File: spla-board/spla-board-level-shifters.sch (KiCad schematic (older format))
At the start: 20 parts, among them J3 J_BODGE, J6 J_SAMPLE, U15 74LVC8T245-Q1, U16 74LVC8T245-Q1, U17 74LVC8T245-Q1, U20 74LVC8T245-Q1, U22 74LVC8T245-Q1, U23 74LVC8T245-Q1, U24 74LVC8T245-Q1, U25 74LVC8T245-Q1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

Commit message: schematic/pch: Remove '-Q1' suffix from 74LVC8T245 chips.
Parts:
- U15, U16, U17, U20, U22, U23, U24, U25, U26, U27, U28, U29, U30, U31, U32: value 74LVC8T245-Q1 -> 74LVC8T245; symbol SPLA:74LVC8T245-Q1 -> SPLA:74LVC8T245
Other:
- note removed: "TODO: Rearrange these pins for PCB layout."
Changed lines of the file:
@@
 FPGA_~PAWR~
 $Comp
-L SPLA:74LVC8T245-Q1 U23
+L SPLA:74LVC8T245 U23
 U 1 1 5E550799
 P 2400 9500
 F 0 "U23" H 2100 8850 50  0000 L CNN
-F 1 "74LVC8T245-Q1" V 2400 9500 50  0000 C CNN
+F 1 "74LVC8T245" V 2400 9500 50  0000 C CNN
 F 2 "Package_SO:TSSOP-24_4.4x7.8mm_P0.65mm" H 2400 8750 50  0001 C CNN
-F 3 "www.ti.com/lit/ds/symlink/txs0108e.pdf" H 2400 9400 50  0001 C CNN
+F 3 "" H 2400 9400 50  0001 C CNN
 	1    2400 9500
 	1    0    0    -1
 $EndComp
 $Comp
-L SPLA:74LVC8T245-Q1 U22
+L SPLA:74LVC8T245 U22
 U 1 1 5E55EB1D
 P 2400 7000
 F 0 "U22" H 2400 7750 50  0000 C CNN
-F 1 "74LVC8T245-Q1" V 2400 6950 50  0000 C CNN
+F 1 "74LVC8T245" V 2400 6950 50  0000 C CNN
 F 2 "Package_SO:TSSOP-24_4.4x7.8mm_P0.65mm" H 2400 5700 50  0001 C CNN
-F 3 "www.ti.com/lit/ds/symlink/txs0108e.pdf" H 2400 7150 50  0001 C CNN
+F 3 "" H 2400 7150 50  0001 C CNN
 	1    2400 7000
 	1    0    0    -1
@@
 FPGA_PA7
 $Comp
-L SPLA:74LVC8T245-Q1 U26
+L SPLA:74LVC8T245 U26
 U 1 1 5E56FCA9
 P 8750 7000
 F 0 "U26" H 8750 7750 50  0000 C CNN
-F 1 "74LVC8T245-Q1" V 8750 6950 50  0000 C CNN
+F 1 "74LVC8T245" V 8750 6950 50  0000 C CNN
 F 2 "Package_SO:TSSOP-24_4.4x7.8mm_P0.65mm" H 8750 5700 50  0001 C CNN
-F 3 "www.ti.com/lit/ds/symlink/txs0108e.pdf" H 8750 7150 50  0001 C CNN
+F 3 "" H 8750 7150 50  0001 C CNN
 	1    8750 7000
 	1    0    0    -1
@@
 Peripheral Bus
 $Comp
-L SPLA:74LVC8T245-Q1 U24
+L SPLA:74LVC8T245 U24
 U 1 1 5E5C1563
 P 6300 7000
 F 0 "U24" H 6300 7750 50  0000 C CNN
-F 1 "74LVC8T245-Q1" V 6300 6950 50  0000 C CNN
+F 1 "74LVC8T245" V 6300 6950 50  0000 C CNN
 F 2 "Package_SO:TSSOP-24_4.4x7.8mm_P0.65mm" H 6300 5700 50  0001 C CNN
-F 3 "www.ti.com/lit/ds/symlink/txs0108e.pdf" H 6300 7150 50  0001 C CNN
+F 3 "" H 6300 7150 50  0001 C CNN
 	1    6300 7000
 	1    0    0    -1
@@
 FPGA_VAA7
 $Comp
-L SPLA:74LVC8T245-Q1 U25
+L SPLA:74LVC8T245 U25
 U 1 1 5E5CA87C
 P 6300 9500
 F 0 "U25" H 6300 10250 50  0000 C CNN
-F 1 "74LVC8T245-Q1" V 6300 9450 50  0000 C CNN
+F 1 "74LVC8T245" V 6300 9450 50  0000 C CNN
 F 2 "Package_SO:TSSOP-24_4.4x7.8mm_P0.65mm" H 6300 8200 50  0001 C CNN
-F 3 "www.ti.com/lit/ds/symlink/txs0108e.pdf" H 6300 9650 50  0001 C CNN
+F 3 "" H 6300 9650 50  0001 C CNN
 	1    6300 9500
 	1    0    0    -1
@@
 TAP_~VBWR~
 $Comp
-L SPLA:74LVC8T245-Q1 U28
+L SPLA:74LVC8T245 U28
 U 1 1 5E61780A
 P 12150 7000
 F 0 "U28" H 12150 7750 50  0000 C CNN
-F 1 "74LVC8T245-Q1" V 12150 6950 50  0000 C CNN
+F 1 "74LVC8T245" V 12150 6950 50  0000 C CNN
 F 2 "Package_SO:TSSOP-24_4.4x7.8mm_P0.65mm" H 12150 5700 50  0001 C CNN
-F 3 "www.ti.com/lit/ds/symlink/txs0108e.pdf" H 12150 7150 50  0001 C CNN
+F 3 "" H 12150 7150 50  0001 C CNN
 	1    12150 7000
 	1    0    0    -1
@@
 FPGA_VDB7
 $Comp
-L SPLA:74LVC8T245-Q1 U29
+L SPLA:74LVC8T245 U29
 U 1 1 5E61D896
 P 14150 7000
 F 0 "U29" H 14150 7750 50  0000 C CNN
-F 1 "74LVC8T245-Q1" V 14150 6950 50  0000 C CNN
+F 1 "74LVC8T245" V 14150 6950 50  0000 C CNN
 F 2 "Package_SO:TSSOP-24_4.4x7.8mm_P0.65mm" H 14150 5700 50  0001 C CNN
-F 3 "www.ti.com/lit/ds/symlink/txs0108e.pdf" H 14150 7150 50  0001 C CNN
+F 3 "" H 14150 7150 50  0001 C CNN
 	1    14150 7000
 	1    0    0    -1
@@
 FPGA_CHR3
 $Comp
-L SPLA:74LVC8T245-Q1 U30
+L SPLA:74LVC8T245 U30
 U 1 1 5E65F50D
 P 14300 1750
 F 0 "U30" H 14000 1100 50  0000 L CNN
-F 1 "74LVC8T245-Q1" V 14300 1750 50  0000 C CNN
+F 1 "74LVC8T245" V 14300 1750 50  0000 C CNN
 F 2 "Package_SO:TSSOP-24_4.4x7.8mm_P0.65mm" H 14300 1000 50  0001 C CNN
-F 3 "www.ti.com/lit/ds/symlink/txs0108e.pdf" H 14300 1650 50  0001 C CNN
+F 3 "" H 14300 1650 50  0001 C CNN
 	1    14300 1750
 	1    0    0    -1
@@
 Inter-PPU Bus\n
 $Comp
-L SPLA:74LVC8T245-Q1 U31
+L SPLA:74LVC8T245 U31
 U 1 1 5E66CF65
 P 14300 4050
 F 0 "U31" H 14000 3400 50  0000 L CNN
-F 1 "74LVC8T245-Q1" V 14300 4050 50  0000 C CNN
+F 1 "74LVC8T245" V 14300 4050 50  0000 C CNN
 F 2 "Package_SO:TSSOP-24_4.4x7.8mm_P0.65mm" H 14300 3300 50  0001 C CNN
-F 3 "www.ti.com/lit/ds/symlink/txs0108e.pdf" H 14300 3950 50  0001 C CNN
+F 3 "" H 14300 3950 50  0001 C CNN
 	1    14300 4050
 	1    0    0    -1
@@
 TAP_PPU2_TST15
 $Comp
-L SPLA:74LVC8T245-Q1 U16
+L SPLA:74LVC8T245 U16
 U 1 1 5E8BF4CB
 P 10650 1750
 F 0 "U16" H 10650 2500 50  0000 C CNN
-F 1 "74LVC8T245-Q1" V 10650 1750 50  0000 C CNN
+F 1 "74LVC8T245" V 10650 1750 50  0000 C CNN
 F 2 "Package_SO:TSSOP-24_4.4x7.8mm_P0.65mm" H 10650 1000 50  0001 C CNN
-F 3 "www.ti.com/lit/ds/symlink/txs0108e.pdf" H 10650 1650 50  0001 C CNN
+F 3 "" H 10650 1650 50  0001 C CNN
 	1    10650 1750
 	1    0    0    -1
 $EndComp
 $Comp
-L SPLA:74LVC8T245-Q1 U17
+L SPLA:74LVC8T245 U17
 U 1 1 5E8C0531
 P 10650 4000
 F 0 "U17" H 10650 4750 50  0000 C CNN
-F 1 "74LVC8T245-Q1" V 10650 4000 50  0000 C CNN
+F 1 "74LVC8T245" V 10650 4000 50  0000 C CNN
 F 2 "Package_SO:TSSOP-24_4.4x7.8mm_P0.65mm" H 10650 3250 50  0001 C CNN
-F 3 "www.ti.com/lit/ds/symlink/txs0108e.pdf" H 10650 3900 50  0001 C CNN
+F 3 "" H 10650 3900 50  0001 C CNN
 	1    10650 4000
 	1    0    0    -1
@@
 TAP_PPU2_EXTLATCH
 $Comp
-L SPLA:74LVC8T245-Q1 U32
+L SPLA:74LVC8T245 U32
 U 1 1 5E6DACCD
 P 6300 1750
 F 0 "U32" H 6300 2500 50  0000 C CNN
-F 1 "74LVC8T245-Q1" V 6300 1750 50  0000 C CNN
+F 1 "74LVC8T245" V 6300 1750 50  0000 C CNN
 F 2 "Package_SO:TSSOP-24_4.4x7.8mm_P0.65mm" H 6300 1000 50  0001 C CNN
-F 3 "www.ti.com/lit/ds/symlink/txs0108e.pdf" H 6300 1650 50  0001 C CNN
+F 3 "" H 6300 1650 50  0001 C CNN
 	1    6300 1750
 	1    0    0    -1
@@
 $EndComp
 $Comp
-L SPLA:74LVC8T245-Q1 U15
+L SPLA:74LVC8T245 U15
 U 1 1 5E8C1D06
 P 6300 4050
 F 0 "U15" H 6300 4800 50  0000 C CNN
-F 1 "74LVC8T245-Q1" V 6300 4050 50  0000 C CNN
+F 1 "74LVC8T245" V 6300 4050 50  0000 C CNN
 F 2 "Package_SO:TSSOP-24_4.4x7.8mm_P0.65mm" H 6300 3300 50  0001 C CNN
-F 3 "www.ti.com/lit/ds/symlink/txs0108e.pdf" H 6300 3950 50  0001 C CNN
+F 3 "" H 6300 3950 50  0001 C CNN
 	1    6300 4050
 	1    0    0    -1
@@
 Wire Wire Line
 	1250 4000 1450 4000
-Text Notes 3600 2850 0    50   ~ 0
-TODO: Rearrange these pins for PCB layout.
 Wire Wire Line
 	3500 1750 2950 1750
@@
 FPGA_BODGE3
 $Comp
-L SPLA:74LVC8T245-Q1 U20
+L SPLA:74LVC8T245 U20
 U 1 1 5E517B3B
 P 2550 1750
 F 0 "U20" H 2550 2500 50  0000 C CNN
-F 1 "74LVC8T245-Q1" V 2550 1750 50  0000 C CNN
+F 1 "74LVC8T245" V 2550 1750 50  0000 C CNN
 F 2 "Package_SO:TSSOP-24_4.4x7.8mm_P0.65mm" H 2550 1000 50  0001 C CNN
-F 3 "www.ti.com/lit/ds/symlink/txs0108e.pdf" H 2550 1650 50  0001 C CNN
+F 3 "" H 2550 1650 50  0001 C CNN
 	1    2550 1750
 	1    0    0    -1
@@
 	10550 5450 10550 11200
 $Comp
-L SPLA:74LVC8T245-Q1 U27
+L SPLA:74LVC8T245 U27
 U 1 1 5E5DCE42
 P 8750 9500
 F 0 "U27" H 8750 10250 50  0000 C CNN
-F 1 "74LVC8T245-Q1" V 8750 9450 50  0000 C CNN
+F 1 "74LVC8T245" V 8750 9450 50  0000 C CNN
 F 2 "Package_SO:TSSOP-24_4.4x7.8mm_P0.65mm" H 8750 8200 50  0001 C CNN
-F 3 "www.ti.com/lit/ds/symlink/txs0108e.pdf" H 8750 9650 50  0001 C CNN
+F 3 "" H 8750 9650 50  0001 C CNN
 	1    8750 9500
 	1    0    0    -1

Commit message: schematic: Add Digikey and ManufacturerId fields to big components.
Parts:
- U15, U16, U17, U20, U22, U23, U24, U25, U26, U27, U28, U29, U30, U31, U32: Digikey (none) -> 296-18593-1-ND; Manufacturer Id (none) -> SN74LVC8T245PWR
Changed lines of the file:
@@
 F 2 "Package_SO:TSSOP-24_4.4x7.8mm_P0.65mm" H 2400 8750 50  0001 C CNN
 F 3 "" H 2400 9400 50  0001 C CNN
+F 4 "296-18593-1-ND" H 2400 9500 50  0001 C CNN "Digikey"
+F 5 "SN74LVC8T245PWR" H 2400 9500 50  0001 C CNN "Manufacturer Id"
 	1    2400 9500
 	1    0    0    -1
@@
 F 2 "Package_SO:TSSOP-24_4.4x7.8mm_P0.65mm" H 2400 5700 50  0001 C CNN
 F 3 "" H 2400 7150 50  0001 C CNN
+F 4 "296-18593-1-ND" H 2400 7000 50  0001 C CNN "Digikey"
+F 5 "SN74LVC8T245PWR" H 2400 7000 50  0001 C CNN "Manufacturer Id"
 	1    2400 7000
 	1    0    0    -1
@@
 F 2 "Package_SO:TSSOP-24_4.4x7.8mm_P0.65mm" H 8750 5700 50  0001 C CNN
 F 3 "" H 8750 7150 50  0001 C CNN
+F 4 "296-18593-1-ND" H 8750 7000 50  0001 C CNN "Digikey"
+F 5 "SN74LVC8T245PWR" H 8750 7000 50  0001 C CNN "Manufacturer Id"
 	1    8750 7000
 	1    0    0    -1
@@
 F 2 "Package_SO:TSSOP-24_4.4x7.8mm_P0.65mm" H 6300 5700 50  0001 C CNN
 F 3 "" H 6300 7150 50  0001 C CNN
+F 4 "296-18593-1-ND" H 6300 7000 50  0001 C CNN "Digikey"
+F 5 "SN74LVC8T245PWR" H 6300 7000 50  0001 C CNN "Manufacturer Id"
 	1    6300 7000
 	1    0    0    -1
@@
 F 2 "Package_SO:TSSOP-24_4.4x7.8mm_P0.65mm" H 6300 8200 50  0001 C CNN
 F 3 "" H 6300 9650 50  0001 C CNN
+F 4 "296-18593-1-ND" H 6300 9500 50  0001 C CNN "Digikey"
+F 5 "SN74LVC8T245PWR" H 6300 9500 50  0001 C CNN "Manufacturer Id"
 	1    6300 9500
 	1    0    0    -1
@@
 F 2 "Package_SO:TSSOP-24_4.4x7.8mm_P0.65mm" H 12150 5700 50  0001 C CNN
 F 3 "" H 12150 7150 50  0001 C CNN
+F 4 "296-18593-1-ND" H 12150 7000 50  0001 C CNN "Digikey"
+F 5 "SN74LVC8T245PWR" H 12150 7000 50  0001 C CNN "Manufacturer Id"
 	1    12150 7000
 	1    0    0    -1
@@
 F 2 "Package_SO:TSSOP-24_4.4x7.8mm_P0.65mm" H 14150 5700 50  0001 C CNN
 F 3 "" H 14150 7150 50  0001 C CNN
+F 4 "296-18593-1-ND" H 14150 7000 50  0001 C CNN "Digikey"
+F 5 "SN74LVC8T245PWR" H 14150 7000 50  0001 C CNN "Manufacturer Id"
 	1    14150 7000
 	1    0    0    -1
@@
 F 2 "Package_SO:TSSOP-24_4.4x7.8mm_P0.65mm" H 14300 1000 50  0001 C CNN
 F 3 "" H 14300 1650 50  0001 C CNN
+F 4 "296-18593-1-ND" H 14300 1750 50  0001 C CNN "Digikey"
+F 5 "SN74LVC8T245PWR" H 14300 1750 50  0001 C CNN "Manufacturer Id"
 	1    14300 1750
 	1    0    0    -1
@@
 F 2 "Package_SO:TSSOP-24_4.4x7.8mm_P0.65mm" H 14300 3300 50  0001 C CNN
 F 3 "" H 14300 3950 50  0001 C CNN
+F 4 "296-18593-1-ND" H 14300 4050 50  0001 C CNN "Digikey"
+F 5 "SN74LVC8T245PWR" H 14300 4050 50  0001 C CNN "Manufacturer Id"
 	1    14300 4050
 	1    0    0    -1
@@
 F 2 "Package_SO:TSSOP-24_4.4x7.8mm_P0.65mm" H 10650 1000 50  0001 C CNN
 F 3 "" H 10650 1650 50  0001 C CNN
+F 4 "296-18593-1-ND" H 10650 1750 50  0001 C CNN "Digikey"
+F 5 "SN74LVC8T245PWR" H 10650 1750 50  0001 C CNN "Manufacturer Id"
 	1    10650 1750
 	1    0    0    -1
@@
 F 2 "Package_SO:TSSOP-24_4.4x7.8mm_P0.65mm" H 10650 3250 50  0001 C CNN
 F 3 "" H 10650 3900 50  0001 C CNN
+F 4 "296-18593-1-ND" H 10650 4000 50  0001 C CNN "Digikey"
+F 5 "SN74LVC8T245PWR" H 10650 4000 50  0001 C CNN "Manufacturer Id"
 	1    10650 4000
 	1    0    0    -1
@@
 F 2 "Package_SO:TSSOP-24_4.4x7.8mm_P0.65mm" H 6300 1000 50  0001 C CNN
 F 3 "" H 6300 1650 50  0001 C CNN
+F 4 "296-18593-1-ND" H 6300 1750 50  0001 C CNN "Digikey"
+F 5 "SN74LVC8T245PWR" H 6300 1750 50  0001 C CNN "Manufacturer Id"
 	1    6300 1750
 	1    0    0    -1
@@
 F 2 "Package_SO:TSSOP-24_4.4x7.8mm_P0.65mm" H 6300 3300 50  0001 C CNN
 F 3 "" H 6300 3950 50  0001 C CNN
+F 4 "296-18593-1-ND" H 6300 4050 50  0001 C CNN "Digikey"
+F 5 "SN74LVC8T245PWR" H 6300 4050 50  0001 C CNN "Manufacturer Id"
 	1    6300 4050
 	1    0    0    -1
@@
 F 2 "Package_SO:TSSOP-24_4.4x7.8mm_P0.65mm" H 2550 1000 50  0001 C CNN
 F 3 "" H 2550 1650 50  0001 C CNN
+F 4 "296-18593-1-ND" H 2550 1750 50  0001 C CNN "Digikey"
+F 5 "SN74LVC8T245PWR" H 2550 1750 50  0001 C CNN "Manufacturer Id"
 	1    2550 1750
 	1    0    0    -1
@@
 F 2 "Package_SO:TSSOP-24_4.4x7.8mm_P0.65mm" H 8750 8200 50  0001 C CNN
 F 3 "" H 8750 9650 50  0001 C CNN
+F 4 "296-18593-1-ND" H 8750 9500 50  0001 C CNN "Digikey"
+F 5 "SN74LVC8T245PWR" H 8750 9500 50  0001 C CNN "Manufacturer Id"
 	1    8750 9500
 	1    0    0    -1

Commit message: schematic: Set 'N/A' for test points and holes 'parts'.
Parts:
- TP1, TP2: Digikey (none) -> N/A; Manufacturer Id (none) -> N/A
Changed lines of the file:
@@
 F 2 "TestPoint:TestPoint_Pad_D1.0mm" H 3700 1550 50  0001 C CNN
 F 3 "~" H 3700 1550 50  0001 C CNN
+F 4 "N/A" H 3500 1550 50  0001 C CNN "Digikey"
+F 5 "N/A" H 3500 1550 50  0001 C CNN "Manufacturer Id"
 	1    3500 1550
 	1    0    0    -1
@@
 F 2 "TestPoint:TestPoint_Pad_D1.0mm" H 1550 1550 50  0001 C CNN
 F 3 "~" H 1550 1550 50  0001 C CNN
+F 4 "N/A" H 1350 1550 50  0001 C CNN "Digikey"
+F 5 "N/A" H 1350 1550 50  0001 C CNN "Manufacturer Id"
 	1    1350 1550
 	1    0    0    -1

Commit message: schematic: Add part numbers for pinheaders (albeit that these are breakaways, and it's not one-per-part).
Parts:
- J3, J6: Digikey (none) -> S1011EC-40-ND; Manufacturer Id (none) -> PRPC040SAAN-RC
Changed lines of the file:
@@
 F 2 "Connector_PinHeader_2.54mm:PinHeader_1x04_P2.54mm_Vertical" H 7950 3950 50  0001 C CNN
 F 3 "~" H 7950 3950 50  0001 C CNN
+F 4 "S1011EC-40-ND" H 7950 3950 50  0001 C CNN "Digikey"
+F 5 "PRPC040SAAN-RC" H 7950 3950 50  0001 C CNN "Manufacturer Id"
 	1    7950 3950
 	1    0    0    -1
@@
 F 2 "Connector_PinHeader_2.54mm:PinHeader_1x04_P2.54mm_Vertical" H 7250 2700 50  0001 C CNN
 F 3 "~" H 7250 2700 50  0001 C CNN
+F 4 "S1011EC-40-ND" H 7250 2700 50  0001 C CNN "Digikey"
+F 5 "PRPC040SAAN-RC" H 7250 2700 50  0001 C CNN "Manufacturer Id"
 	1    7250 2700
 	0    -1   1    0

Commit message: bom: Add manufacturers.
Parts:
- J3, J6: Manufacturer (none) -> Sullins Connector Solutions
- TP1, TP2: Manufacturer (none) -> N/A
- U15, U16, U17, U20, U22, U23, U24, U25, U26, U27, U28, U29, U30, U31, U32: Manufacturer (none) -> Texas Instruments
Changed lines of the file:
@@
 F 4 "296-18593-1-ND" H 2400 9500 50  0001 C CNN "Digikey"
 F 5 "SN74LVC8T245PWR" H 2400 9500 50  0001 C CNN "Manufacturer Id"
+F 6 "Texas Instruments" H 2400 9500 50  0001 C CNN "Manufacturer"
 	1    2400 9500
 	1    0    0    -1
@@
 F 4 "296-18593-1-ND" H 2400 7000 50  0001 C CNN "Digikey"
 F 5 "SN74LVC8T245PWR" H 2400 7000 50  0001 C CNN "Manufacturer Id"
+F 6 "Texas Instruments" H 2400 7000 50  0001 C CNN "Manufacturer"
 	1    2400 7000
 	1    0    0    -1
@@
 F 4 "296-18593-1-ND" H 8750 7000 50  0001 C CNN "Digikey"
 F 5 "SN74LVC8T245PWR" H 8750 7000 50  0001 C CNN "Manufacturer Id"
+F 6 "Texas Instruments" H 8750 7000 50  0001 C CNN "Manufacturer"
 	1    8750 7000
 	1    0    0    -1
@@
 F 4 "296-18593-1-ND" H 6300 7000 50  0001 C CNN "Digikey"
 F 5 "SN74LVC8T245PWR" H 6300 7000 50  0001 C CNN "Manufacturer Id"
+F 6 "Texas Instruments" H 6300 7000 50  0001 C CNN "Manufacturer"
 	1    6300 7000
 	1    0    0    -1
@@
 F 4 "296-18593-1-ND" H 6300 9500 50  0001 C CNN "Digikey"
 F 5 "SN74LVC8T245PWR" H 6300 9500 50  0001 C CNN "Manufacturer Id"
+F 6 "Texas Instruments" H 6300 9500 50  0001 C CNN "Manufacturer"
 	1    6300 9500
 	1    0    0    -1
@@
 F 4 "296-18593-1-ND" H 12150 7000 50  0001 C CNN "Digikey"
 F 5 "SN74LVC8T245PWR" H 12150 7000 50  0001 C CNN "Manufacturer Id"
+F 6 "Texas Instruments" H 12150 7000 50  0001 C CNN "Manufacturer"
 	1    12150 7000
 	1    0    0    -1
@@
 F 4 "296-18593-1-ND" H 14150 7000 50  0001 C CNN "Digikey"
 F 5 "SN74LVC8T245PWR" H 14150 7000 50  0001 C CNN "Manufacturer Id"
+F 6 "Texas Instruments" H 14150 7000 50  0001 C CNN "Manufacturer"
 	1    14150 7000
 	1    0    0    -1
@@
 F 4 "296-18593-1-ND" H 14300 1750 50  0001 C CNN "Digikey"
 F 5 "SN74LVC8T245PWR" H 14300 1750 50  0001 C CNN "Manufacturer Id"
+F 6 "Texas Instruments" H 14300 1750 50  0001 C CNN "Manufacturer"
 	1    14300 1750
 	1    0    0    -1
@@
 F 4 "296-18593-1-ND" H 14300 4050 50  0001 C CNN "Digikey"
 F 5 "SN74LVC8T245PWR" H 14300 4050 50  0001 C CNN "Manufacturer Id"
+F 6 "Texas Instruments" H 14300 4050 50  0001 C CNN "Manufacturer"
 	1    14300 4050
 	1    0    0    -1
@@
 F 4 "296-18593-1-ND" H 10650 1750 50  0001 C CNN "Digikey"
 F 5 "SN74LVC8T245PWR" H 10650 1750 50  0001 C CNN "Manufacturer Id"
+F 6 "Texas Instruments" H 10650 1750 50  0001 C CNN "Manufacturer"
 	1    10650 1750
 	1    0    0    -1
@@
 F 4 "296-18593-1-ND" H 10650 4000 50  0001 C CNN "Digikey"
 F 5 "SN74LVC8T245PWR" H 10650 4000 50  0001 C CNN "Manufacturer Id"
+F 6 "Texas Instruments" H 10650 4000 50  0001 C CNN "Manufacturer"
 	1    10650 4000
 	1    0    0    -1
@@
 F 4 "296-18593-1-ND" H 6300 1750 50  0001 C CNN "Digikey"
 F 5 "SN74LVC8T245PWR" H 6300 1750 50  0001 C CNN "Manufacturer Id"
+F 6 "Texas Instruments" H 6300 1750 50  0001 C CNN "Manufacturer"
 	1    6300 1750
 	1    0    0    -1
@@
 F 4 "N/A" H 3500 1550 50  0001 C CNN "Digikey"
 F 5 "N/A" H 3500 1550 50  0001 C CNN "Manufacturer Id"
+F 6 "N/A" H 3500 1550 50  0001 C CNN "Manufacturer"
 	1    3500 1550
 	1    0    0    -1
@@
 F 4 "296-18593-1-ND" H 6300 4050 50  0001 C CNN "Digikey"
 F 5 "SN74LVC8T245PWR" H 6300 4050 50  0001 C CNN "Manufacturer Id"
+F 6 "Texas Instruments" H 6300 4050 50  0001 C CNN "Manufacturer"
 	1    6300 4050
 	1    0    0    -1
@@
 F 4 "S1011EC-40-ND" H 7950 3950 50  0001 C CNN "Digikey"
 F 5 "PRPC040SAAN-RC" H 7950 3950 50  0001 C CNN "Manufacturer Id"
+F 6 "Sullins Connector Solutions" H 7950 3950 50  0001 C CNN "Manufacturer"
 	1    7950 3950
 	1    0    0    -1
@@
 F 4 "296-18593-1-ND" H 2550 1750 50  0001 C CNN "Digikey"
 F 5 "SN74LVC8T245PWR" H 2550 1750 50  0001 C CNN "Manufacturer Id"
+F 6 "Texas Instruments" H 2550 1750 50  0001 C CNN "Manufacturer"
 	1    2550 1750
 	1    0    0    -1
@@
 F 4 "N/A" H 1350 1550 50  0001 C CNN "Digikey"
 F 5 "N/A" H 1350 1550 50  0001 C CNN "Manufacturer Id"
+F 6 "N/A" H 1350 1550 50  0001 C CNN "Manufacturer"
 	1    1350 1550
 	1    0    0    -1
@@
 F 4 "296-18593-1-ND" H 8750 9500 50  0001 C CNN "Digikey"
 F 5 "SN74LVC8T245PWR" H 8750 9500 50  0001 C CNN "Manufacturer Id"
+F 6 "Texas Instruments" H 8750 9500 50  0001 C CNN "Manufacturer"
 	1    8750 9500
 	1    0    0    -1
@@
 F 4 "S1011EC-40-ND" H 7250 2700 50  0001 C CNN "Digikey"
 F 5 "PRPC040SAAN-RC" H 7250 2700 50  0001 C CNN "Manufacturer Id"
+F 6 "Sullins Connector Solutions" H 7250 2700 50  0001 C CNN "Manufacturer"
 	1    7250 2700
 	0    -1   1    0

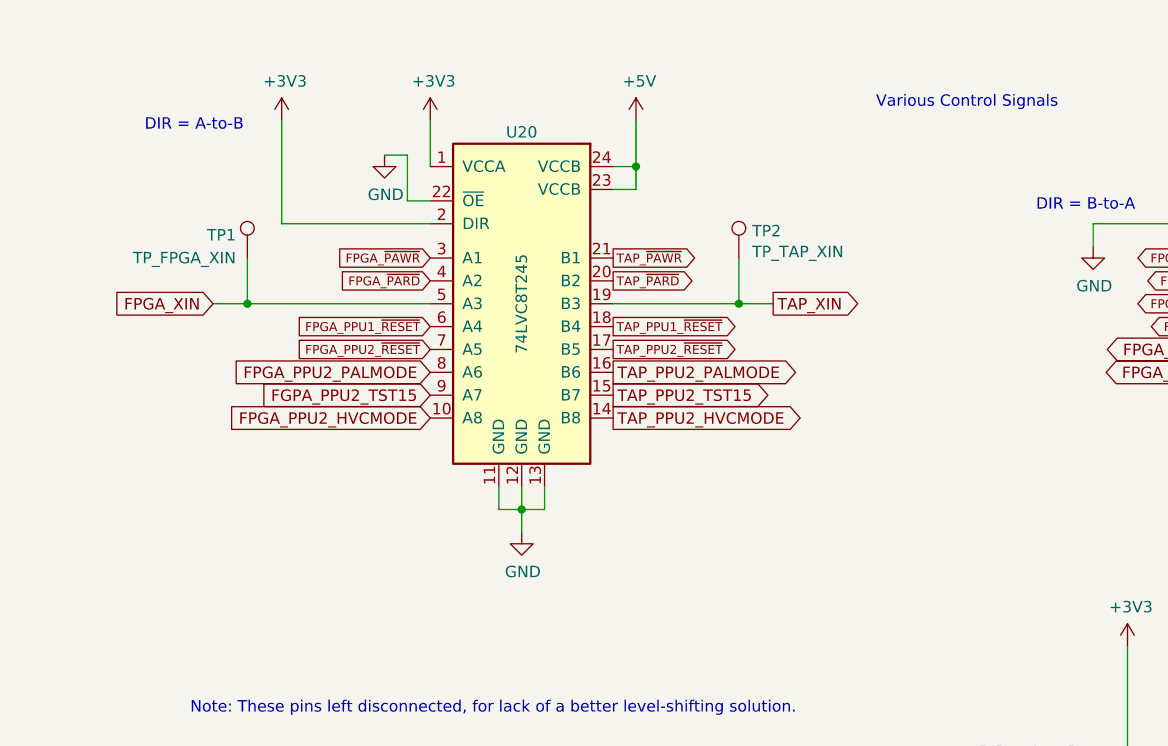
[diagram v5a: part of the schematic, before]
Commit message: schematic/pcb: Move PPU RESET pulldowns before level shifter.
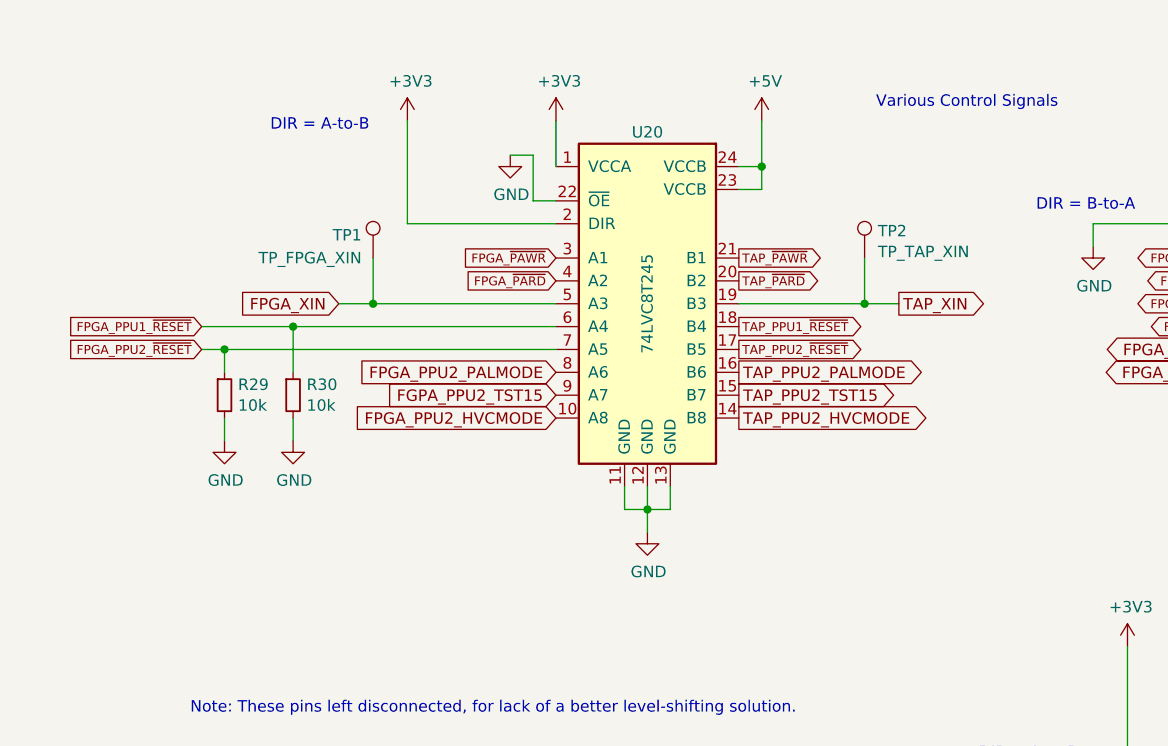
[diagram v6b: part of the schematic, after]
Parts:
- added R29, R30: 10k, Resistor_SMD:R_0603_1608Metric, symbol Device:R_Small
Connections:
- net FPGA_PPU1_~RESET~: now also R30.1
- net FPGA_PPU2_~RESET~: now also R29.1
- net GND: now also R29.2, R30.2
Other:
- moved on the sheet: TP1, TP2, U20
